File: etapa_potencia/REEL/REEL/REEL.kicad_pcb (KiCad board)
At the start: 2 copper layers, 95.2 x 60 mm, 46 parts, among them J1 Conn_display2, J2 Conn_display_2, J3 Conn_teclado, J4 Conn_audio, J5 USB_B_Mini, J6 Salida_audio, SW1 SW_Push, SW3 SW_Push, SW4 BW, SW5 FW, U1 Tp5400, U2 ESP32-WROOM-32, U3 FT232, U4 AMS1117-3.3

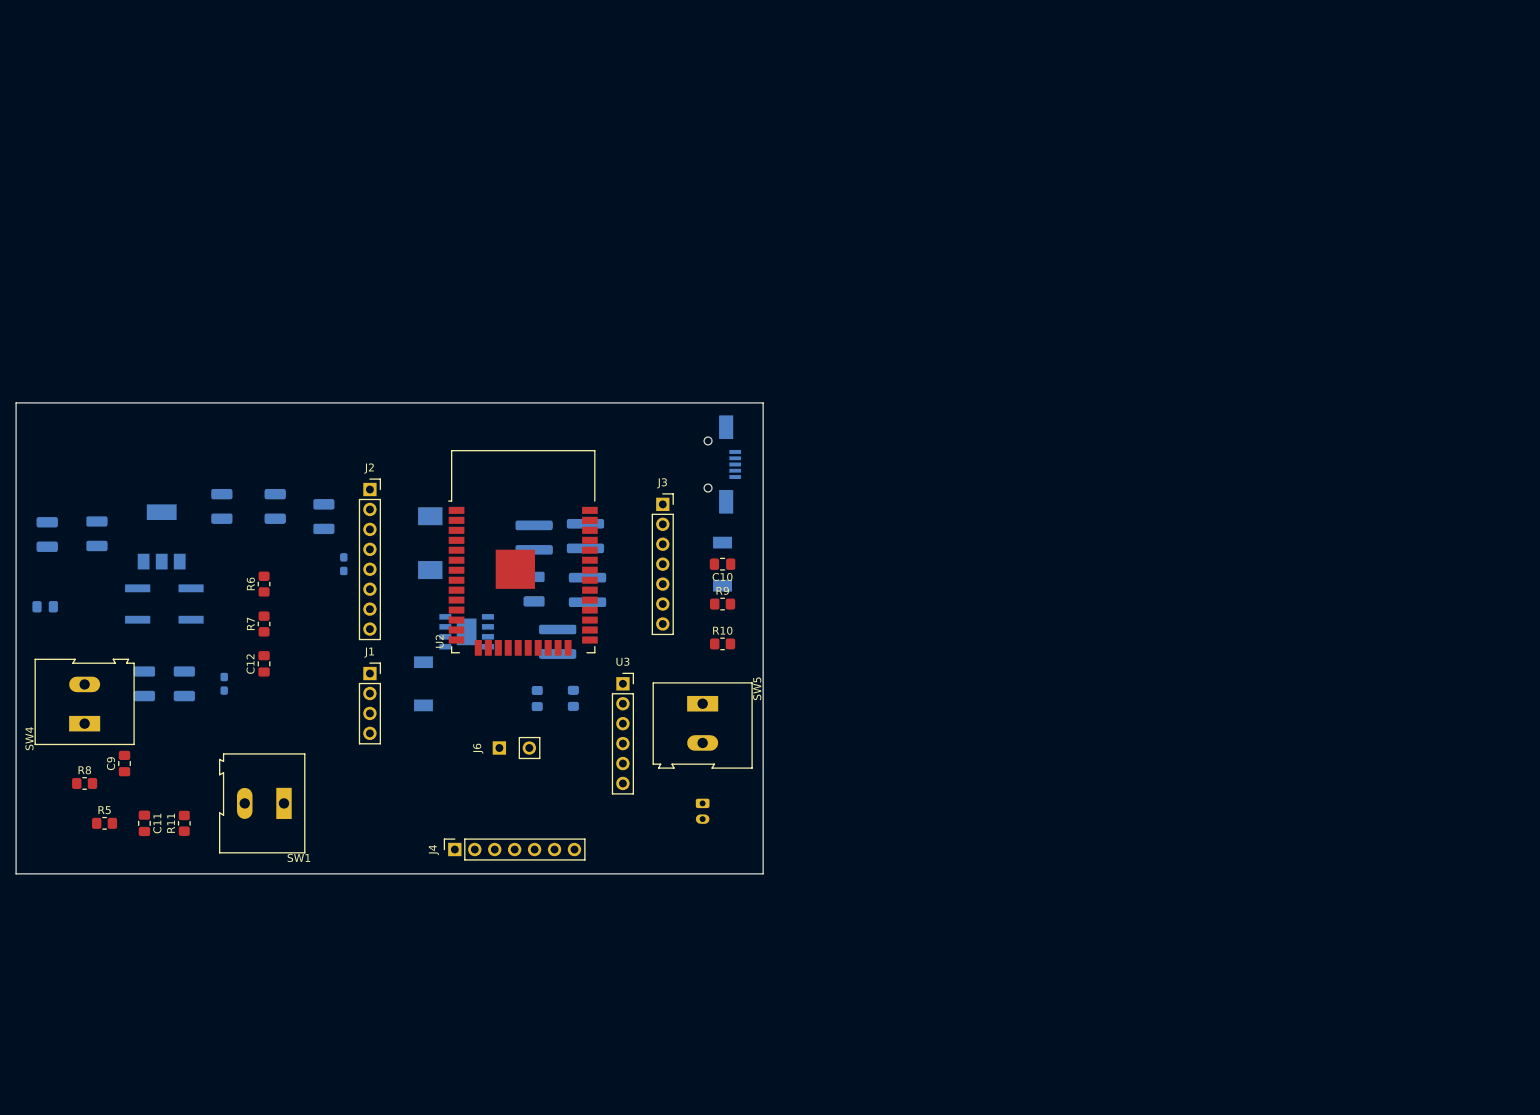
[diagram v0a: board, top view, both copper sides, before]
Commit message: Reorganización pcb
Después de primera revisión del profe Camargo
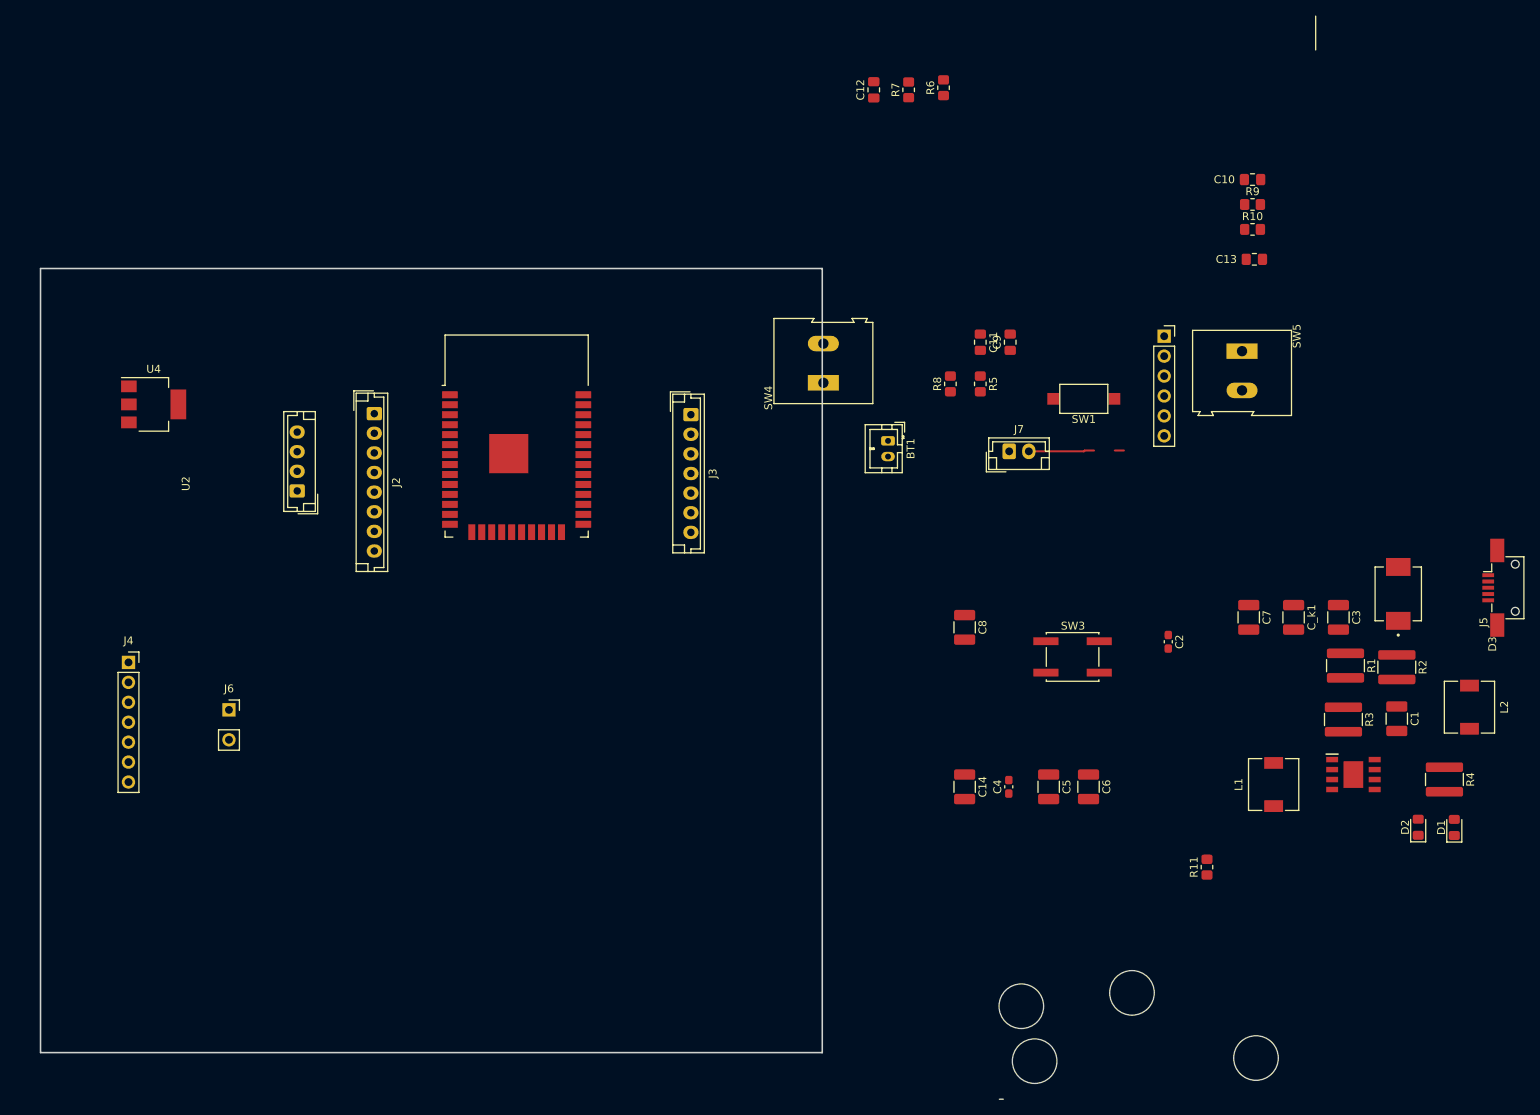
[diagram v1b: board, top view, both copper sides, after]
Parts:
- added J7: Entrada_buzzer, Connector_JST:JST_EH_B2B-EH-A_1x02_P2.50mm_Vertical, F.Cu at (153.4, 79.6)
- BT1, C1, C13, C14, C2, C3, C4, C5, C6, C7, C8, C_k1, D1, D2, D3, J5, L1, L2, R1, R2, R3, R4, SW3, U1, U4: moved to F.Cu
- J1: footprint Connector_PinSocket_2.54mm:PinSocket_1x04_P2.54mm_Vertical -> Connector_JST:JST_EH_B4B-EH-A_1x04_P2.50mm_Vertical
- J2: footprint Connector_PinSocket_2.54mm:PinSocket_1x08_P2.54mm_Vertical -> Connector_JST:JST_EH_B8B-EH-A_1x08_P2.50mm_Vertical
- J3: footprint Connector_PinSocket_2.54mm:PinSocket_1x07_P2.54mm_Vertical -> Connector_JST:JST_EH_B7B-EH-A_1x07_P2.50mm_Vertical
- J6: value Salida_audio -> Salida_amp
- SW1: footprint TerminalBlock:TerminalBlock_Altech_AK300-2_P5.00mm -> Button_Switch_SMD:SW_SPST_CK_RS282G05A3
- moved C13 160.3 mm to (184.6, 55.1), turned to 0 degrees
- moved C7 131.6 mm to (183.9, 100.8)
- moved C_k1 130.5 mm to (189.6, 100.8)
- moved R11 130.4 mm to (178.6, 132.6)
- moved C3 129.9 mm to (195.3, 100.8)
- moved C9 125.0 mm to (153.5, 65.7)
- moved R5 124.8 mm to (149.7, 71.0), turned to -90 degrees
- moved D3 123.5 mm to (202.9, 97.8)
- moved C11 122.9 mm to (149.7, 65.7)
- moved R8 121.5 mm to (145.9, 71.0), turned to 90 degrees
- moved C14 121.2 mm to (147.7, 122.3)
- moved C6 121.0 mm to (163.5, 122.3)
- moved D1 118.0 mm to (210.1, 127.5)
- moved SW3 115.9 mm to (161.4, 105.8), turned to 0 degrees
- moved U1 114.4 mm to (197.2, 120.8), turned to 0 degrees
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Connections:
- BT1 pad 1: +5V -> Net-(BT1-Pad1)
- C1 pad 1: +5V -> Net-(C1-Pad1)
- C4 pad 1: +5V -> Net-(BT1-Pad1)
- C5 pad 1: +5V -> Net-(BT1-Pad1)
- C6 pad 1: +5V -> Net-(BT1-Pad1)
- D3 pad A: +5V -> /Power/5V
- J4 pad 3: unconnected-(J4-Pad3) -> /SD_MODE
- J6 pad 1: unconnected-(J6-Pad1) -> Net-(J6-Pad1)
- J6 pad 2: unconnected-(J6-Pad2) -> Net-(J6-Pad2)
- L1 pad 1: +5V -> /Power/5V
- L1 pad 2: +5V -> Net-(BT1-Pad1)
- R1 pad 2: +5V -> Net-(C1-Pad1)
- R2 pad 2: +5V -> Net-(C1-Pad1)
- R3 pad 1: +5V -> Net-(C1-Pad1)
- U1 pad 5: +5V -> Net-(C1-Pad1)
- U1 pad 6: +5V -> Net-(BT1-Pad1)
- U1 pad 8: +5V -> /Power/5V
- U2 pad 16: unconnected-(U2-Pad16) -> /SD_MODE
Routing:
- net Net-(J6-Pad2): track 0.00 -> 8.35 mm
- net (no net): track 0.00 -> 1.18 mm
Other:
- board size 95.2 x 60 mm -> 157.7 x 105.8 mm

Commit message: Ordenar huellas en PCB ahora sí
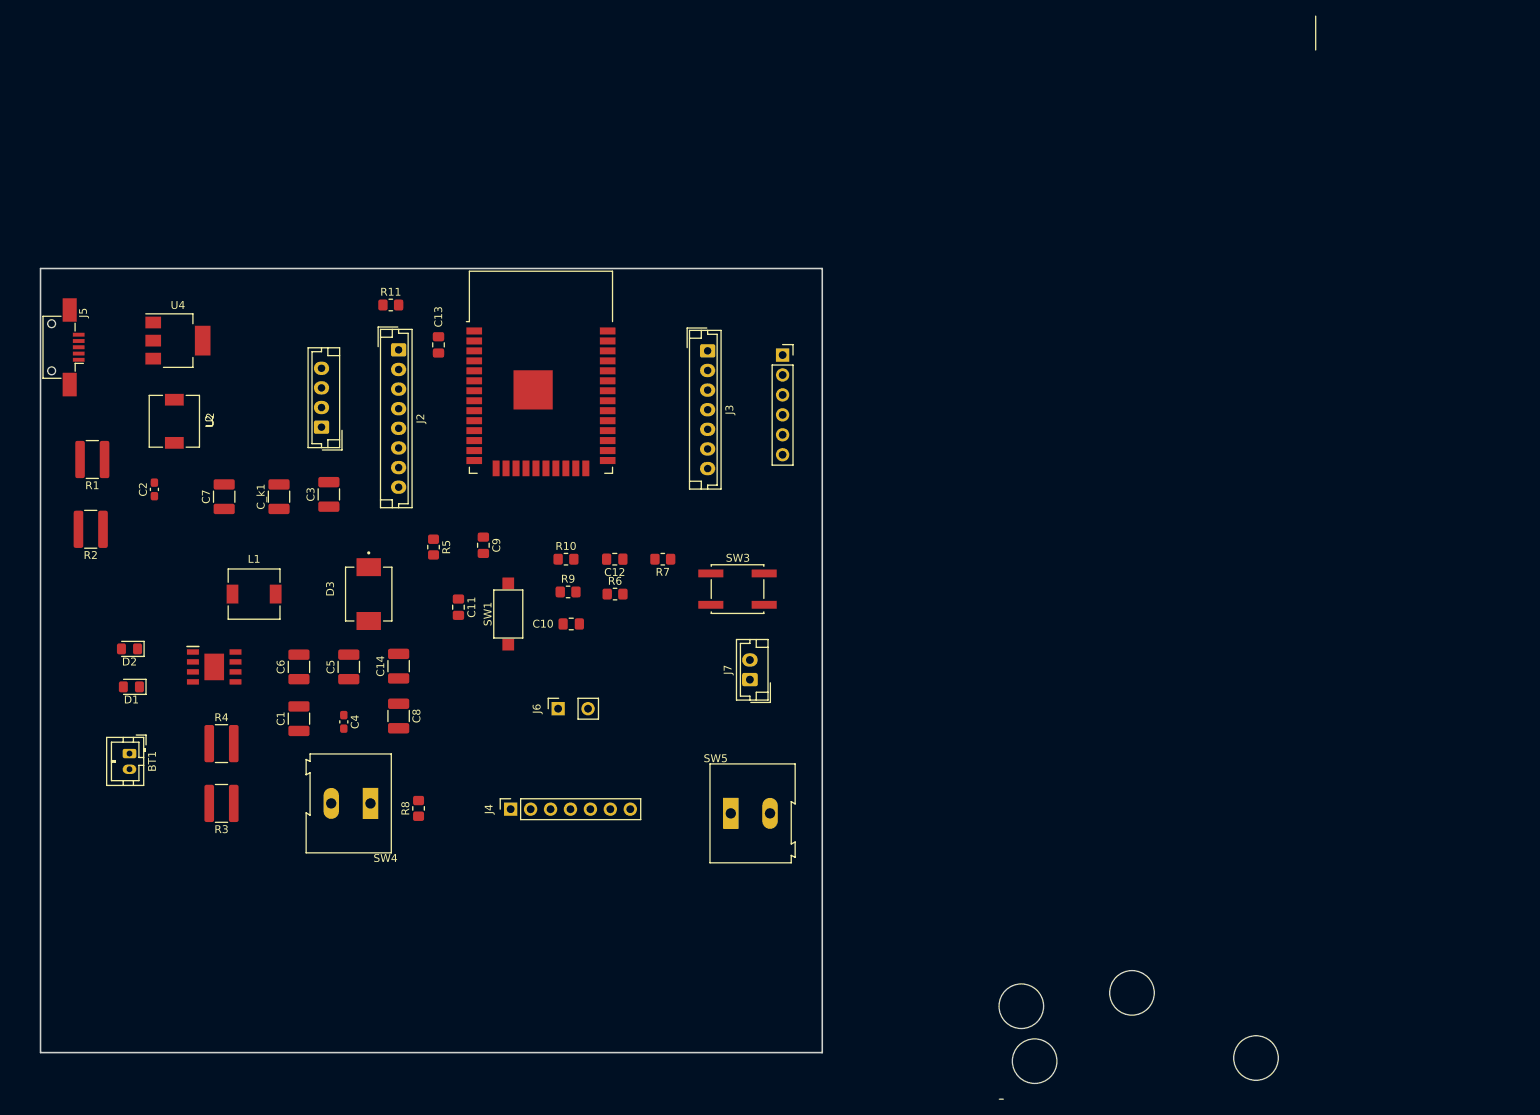
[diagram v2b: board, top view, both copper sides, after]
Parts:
- moved J5 185.3 mm to (33.2, 66.3), turned to 180 degrees
- moved D1 169.5 mm to (41.5, 109.6), turned to 180 degrees
- moved L2 169.0 mm to (47.0, 75.8)
- moved R2 167.3 mm to (36.3, 89.5), turned to 180 degrees
- moved D2 165.8 mm to (41.3, 104.8), turned to 180 degrees
- moved R1 161.8 mm to (36.5, 80.6), turned to 180 degrees
- moved R4 155.9 mm to (53.0, 116.8), turned to 0 degrees
- moved U1 145.8 mm to (52.1, 107.1)
- moved R3 143.3 mm to (53.0, 124.5), turned to 180 degrees
- moved C1 139.9 mm to (62.9, 113.7), turned to 90 degrees
- moved L1 132.1 mm to (57.1, 97.8), turned to 0 degrees
- moved C7 131.4 mm to (53.3, 85.4), turned to 90 degrees
- moved D3 131.2 mm to (71.8, 97.8), turned to -90 degrees
- moved C2 130.6 mm to (44.5, 84.5), turned to 90 degrees
- moved C_k1 130.2 mm to (60.3, 85.4), turned to 90 degrees
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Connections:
- U2 pad 12: /T2 -> /SDMISO
- U2 pad 14: /T3 -> /FW
- U2 pad 33: /SDMISO -> /T3
- U2 pad 36: /T1 -> /T2
- U2 pad 37: /FW -> /T1
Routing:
- net Net-(J6-Pad2): track 8.35 -> 0.00 mm
- net (no net): track 1.18 -> 0.00 mm

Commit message: PCB lista para rutear
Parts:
- moved FW 18.5 mm to (109.6, 109.2)
- moved MicroUSB 9.53 mm to (38.9, 74.0)
- moved R2 9.53 mm to (42.1, 97.2)
- moved R1 9.53 mm to (42.3, 88.3)
- moved Battery 4.95 mm to (42.5, 113.3)
- moved Buzzer 4.48 mm to (124.8, 108.6)
- moved C2 3.81 mm to (48.3, 84.5)
- moved L2 3.81 mm to (50.8, 75.8)
- moved U4 3.81 mm to (51.3, 65.5)
- moved D3 3.78 mm to (73.0, 94.2)
- moved C1 3.78 mm to (64.1, 110.1)
- moved L1 3.78 mm to (58.4, 94.2)
- moved C4 3.78 mm to (69.8, 110.5)
- moved C8 3.78 mm to (76.8, 109.8)
- moved C6 3.78 mm to (64.1, 103.5)
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- renumbered SW4 to BW, BT1 to Battery, J7 to Buzzer, J2 to Display, SW1 to Enable, SW5 to FW, J3 to Keyboard, J5 to MicroUSB, SW3 to Prog, U3 to Programmer, J1 to SD
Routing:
- added copper zone on B.Cu, net GND
- added copper zone on F.Cu, net GND
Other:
- board size 157.7 x 105.8 mm -> 117 x 107.1 mm
- board text added: "Amplifier"

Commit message: Cambio orden pines etapa de audio
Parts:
- renumbered Battery to BT1, SD to J1, Display to J2, Keyboard to J3, MicroUSB to J5, Buzzer to J7, Enable to SW1, Prog to SW3, BW to SW4, FW to SW5, Programmer to U3
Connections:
- J4 pad 1: +3V3 -> /I2S_WS
- J4 pad 2: GND -> /I2S_CLK
- J4 pad 3: /SD_MODE -> /I2S_DIN
- J4 pad 5: /I2S_DIN -> /I2S_SD
- J4 pad 6: /I2S_CLK -> GND
- J4 pad 7: /I2S_WS -> +3V3
- U2 pad 16: /SD_MODE -> /I2S_SD
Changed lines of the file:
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@@
   (net 53 "Net-(C1-Pad1)")
   (net 54 "/Power/5V")
-  (net 55 "/SD_MODE")
+  (net 55 "/I2S_SD")
   (net 56 "unconnected-(J4-Pad4)")
   (net 57 "Net-(J6-Pad1)")
@@
     (property "Sheetname" "")
     (attr through_hole)
-    (fp_text reference "FW" (at 2.13 -7.62) (layer "F.SilkS")
+    (fp_text reference "SW5" (at 2.13 -7.62) (layer "F.SilkS")
       (effects (font (size 1 1) (thickness 0.15)))
     )
@@
   )
   (footprint "Connector_PinSocket_2.54mm:PinSocket_1x07_P2.54mm_Vertical" (layer "F.Cu")
-    (at 86.36 123.825 90)
+    (at 86.360002 123.824998 90)
     (descr "Through hole straight socket strip, 1x07, 2.54mm pitch, single row (from Kicad 4.0.7), script generated")
     (tags "Through hole socket strip THT 1x07 2.54mm single row")
@@
     (fp_line (start 0.635 -1.27) (end 1.27 -0.635) (layer "F.Fab") (width 0.1))
     (pad "1" thru_hole rect (at 0 0 90) (size 1.7 1.7) (drill 1) (layers *.Cu *.Mask)
-      (net 5 "+3V3") (pinfunction "Pin_1") (pintype "passive"))
+      (net 37 "/I2S_WS") (pinfunction "Pin_1") (pintype "passive"))
     (pad "2" thru_hole oval (at 0 2.54 90) (size 1.7 1.7) (drill 1) (layers *.Cu *.Mask)
-      (net 2 "GND") (pinfunction "Pin_2") (pintype "passive"))
+      (net 36 "/I2S_CLK") (pinfunction "Pin_2") (pintype "passive"))
     (pad "3" thru_hole oval (at 0 5.08 90) (size 1.7 1.7) (drill 1) (layers *.Cu *.Mask)
-      (net 55 "/SD_MODE") (pinfunction "Pin_3") (pintype "passive"))
+      (net 35 "/I2S_DIN") (pinfunction "Pin_3") (pintype "passive"))
     (pad "4" thru_hole oval (at 0 7.62 90) (size 1.7 1.7) (drill 1) (layers *.Cu *.Mask)
       (net 56 "unconnected-(J4-Pad4)") (pinfunction "Pin_4") (pintype "passive+no_connect"))
     (pad "5" thru_hole oval (at 0 10.16 90) (size 1.7 1.7) (drill 1) (layers *.Cu *.Mask)
-      (net 35 "/I2S_DIN") (pinfunction "Pin_5") (pintype "passive"))
+      (net 55 "/I2S_SD") (pinfunction "Pin_5") (pintype "passive"))
     (pad "6" thru_hole oval (at 0 12.7 90) (size 1.7 1.7) (drill 1) (layers *.Cu *.Mask)
-      (net 36 "/I2S_CLK") (pinfunction "Pin_6") (pintype "passive"))
+      (net 2 "GND") (pinfunction "Pin_6") (pintype "passive"))
     (pad "7" thru_hole oval (at 0 15.24 90) (size 1.7 1.7) (drill 1) (layers *.Cu *.Mask)
-      (net 37 "/I2S_WS") (pinfunction "Pin_7") (pintype "passive"))
+      (net 5 "+3V3") (pinfunction "Pin_7") (pintype "passive"))
     (model "${KICAD6_3DMODEL_DIR}/Connector_PinSocket_2.54mm.3dshapes/PinSocket_1x07_P2.54mm_Vertical.wrl"
       (offset (xyz 0 0 0))
@@
     (property "Sheetname" "")
     (attr through_hole)
-    (fp_text reference "SD" (at -4.124 0.254) (layer "F.SilkS")
+    (fp_text reference "J1" (at -4.124 0.254) (layer "F.SilkS")
       (effects (font (size 1 1) (thickness 0.15)))
     )
@@
   )
   (footprint "Connector_PinSocket_2.54mm:PinSocket_1x02_P2.54mm_Vertical" (layer "F.Cu")
-    (at 93.6752 111.0234 90)
+    (at 93.675202 111.023398 90)
     (descr "Through hole straight socket strip, 1x02, 2.54mm pitch, single row (from Kicad 4.0.7), script generated")
     (tags "Through hole socket strip THT 1x02 2.54mm single row")
@@
     (property "Sheetname" "")
     (attr through_hole)
-    (fp_text reference "BW" (at 9.75 0.245 90) (layer "F.SilkS")
+    (fp_text reference "SW4" (at 9.75 0.245 90) (layer "F.SilkS")
       (effects (font (size 1 1) (thickness 0.15)))
     )
@@
     (property "Sheetname" "")
     (attr through_hole)
-    (fp_text reference "Display" (at 8.75 -2.8 90) (layer "F.SilkS")
+    (fp_text reference "J2" (at 8.75 -2.8 90) (layer "F.SilkS")
       (effects (font (size 1 1) (thickness 0.15)))
     )
@@
     (property "Sheetname" "")
     (attr through_hole)
-    (fp_text reference "Keyboard" (at 6.858 3.81 90) (layer "F.SilkS")
+    (fp_text reference "J3" (at 6.858 3.81 90) (layer "F.SilkS")
       (effects (font (size 1 1) (thickness 0.15)))
     )
@@
     (property "Sheetname" "")
     (attr smd)
-    (fp_text reference "Prog" (at 0.05 -3.95) (layer "F.SilkS")
+    (fp_text reference "SW3" (at 0.05 -3.95) (layer "F.SilkS")
       (effects (font (size 1 1) (thickness 0.15)))
     )
@@
       (net 2 "GND") (pinfunction "GND") (pintype "passive"))
     (pad "16" smd rect (at -4.445 9.255 90) (size 2 0.9) (layers "F.Cu" "F.Paste" "F.Mask")
-      (net 55 "/SD_MODE") (pinfunction "IO13") (pintype "bidirectional"))
+      (net 55 "/I2S_SD") (pinfunction "IO13") (pintype "bidirectional"))
     (pad "17" smd rect (at -3.175 9.255 90) (size 2 0.9) (layers "F.Cu" "F.Paste" "F.Mask")
       (net 17 "unconnected-(U2-Pad17)") (pinfunction "SHD/SD2") (pintype "bidirectional+no_connect"))
@@
     (property "Sheetname" "")
     (attr through_hole)
-    (fp_text reference "Programmer" (at -3.2 6.325 90) (layer "F.SilkS")
+    (fp_text reference "U3" (at -3.2 6.325 90) (layer "F.SilkS")
       (effects (font (size 1 1) (thickness 0.15)))
     )
@@
     (property "Sheetname" "")
     (attr through_hole)
-    (fp_text reference "Buzzer" (at 1.25 -2.8 90) (layer "F.SilkS")
+    (fp_text reference "J7" (at 1.25 -2.8 90) (layer "F.SilkS")
       (effects (font (size 1 1) (thickness 0.15)))
     )
@@
     (property "Sheetname" "Power")
     (attr smd)
-    (fp_text reference "MicroUSB" (at -3.625 -0.33 90) (layer "F.SilkS")
+    (fp_text reference "J5" (at -3.625 -0.33 90) (layer "F.SilkS")
       (effects (font (size 1 1) (thickness 0.15)))
     )
@@
     (property "Sheetname" "Power")
     (attr through_hole)
-    (fp_text reference "Battery" (at 1 -2.9 90) (layer "F.SilkS")
+    (fp_text reference "BT1" (at 1 -2.9 90) (layer "F.SilkS")
       (effects (font (size 1 1) (thickness 0.15)))
     )
@@
     (property "Sheetname" "")
     (attr smd)
-    (fp_text reference "Enable" (at 0 -2.6 90) (layer "F.SilkS")
-      (effects (font (size 1 1) (thickness 0.15)))
-    )
+    (fp_text reference "SW1" (at 0 -2.6 90) (layer "F.SilkS")
+      (effects (font (size 1 1) (thickness 0.15)))
+    )

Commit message: Primer ruteo PCB
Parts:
- moved R8 4.69 mm to (79.4, 116.8), turned to -90 degrees
- renumbered SW4 to BW, BT1 to Battery, J7 to Buzzer, SW1 to Enable, SW5 to FW, J3 to Keyboard, J2 to LCD, J5 to MicroUSB, SW3 to Prog, U3 to Programmer, J1 to SD
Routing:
- net +3V3: track 0.00 -> 150.3 mm, vias 0 -> 2
- net /I2S_CLK: track 0.00 -> 66.9 mm, vias 0 -> 2
- net +5V: track 0.00 -> 66.5 mm
- net Net-(C1-Pad1): track 0.00 -> 64.4 mm, vias 0 -> 2
- net /I2S_WS: track 0.00 -> 58.3 mm, vias 0 -> 2
- net Net-(BT1-Pad1): track 0.00 -> 53.3 mm, vias 0 -> 1
- net /EN: track 0.00 -> 53.3 mm, vias 0 -> 4
- net /I2S_DIN: track 0.00 -> 46.7 mm, vias 0 -> 1
- net /I2S_SD: track 0.00 -> 46.4 mm, vias 0 -> 1
- net /BW: track 0.00 -> 45.4 mm
- net /SDMISO: track 0.00 -> 41.0 mm, vias 0 -> 2
- net Net-(J6-Pad1): track 0.00 -> 37.2 mm
- net Net-(J6-Pad2): track 0.00 -> 32.3 mm
- net /SDCS: track 0.00 -> 30.8 mm, vias 0 -> 2
- net /RX_D0: track 0.00 -> 30.5 mm, vias 0 -> 2
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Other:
- board size 117 x 107.1 mm -> 93.2 x 73.9 mm

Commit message: Adición conector de tarjeta SD
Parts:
- J1: renamed from SD; footprint Connector_JST:JST_EH_B4B-EH-A_1x04_P2.50mm_Vertical -> Connector_PinHeader_2.54mm:PinHeader_1x06_P2.54mm_Vertical
- moved J1 12.1 mm to (70.5, 65.4), turned to -90 degrees
- renumbered Battery to BT1, LCD to J2, Keyboard to J3, MicroUSB to J5, Buzzer to J7, Enable to SW1, Prog to SW3, BW to SW4, FW to SW5, Programmer to U3
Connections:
- J1 pad 1: /SDCS -> +3V3
- J1 pad 2: /MOSI -> /SDCS
- J1 pad 3: /SDMISO -> /MOSI
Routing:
- net /SDCS: track 30.8 -> 41.5 mm, vias 2 -> 4
- net /SDMISO: track 41.0 -> 46.2 mm
- net /SCK: track 20.6 -> 25.0 mm
- net /MOSI: track 20.5 -> 23.2 mm, vias 0 -> 2
- net +3V3: track 150.3 -> 152.9 mm
